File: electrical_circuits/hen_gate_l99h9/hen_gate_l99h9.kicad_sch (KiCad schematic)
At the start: 4 parts, among them U1 L99H02XP

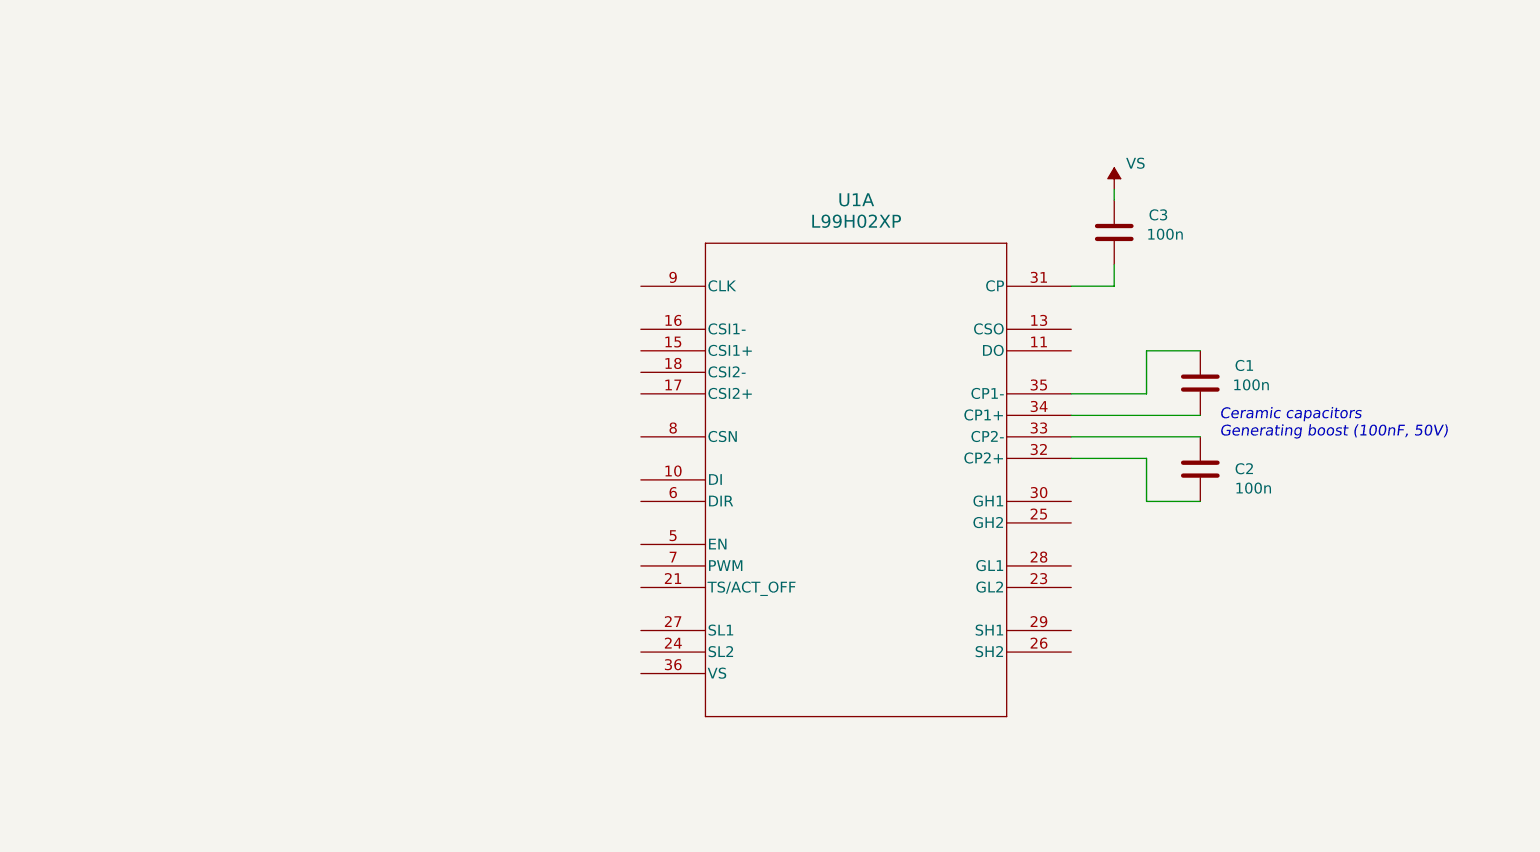
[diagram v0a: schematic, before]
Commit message: Chosen MOSFET transistors and other elements for LT1158 gate driver.
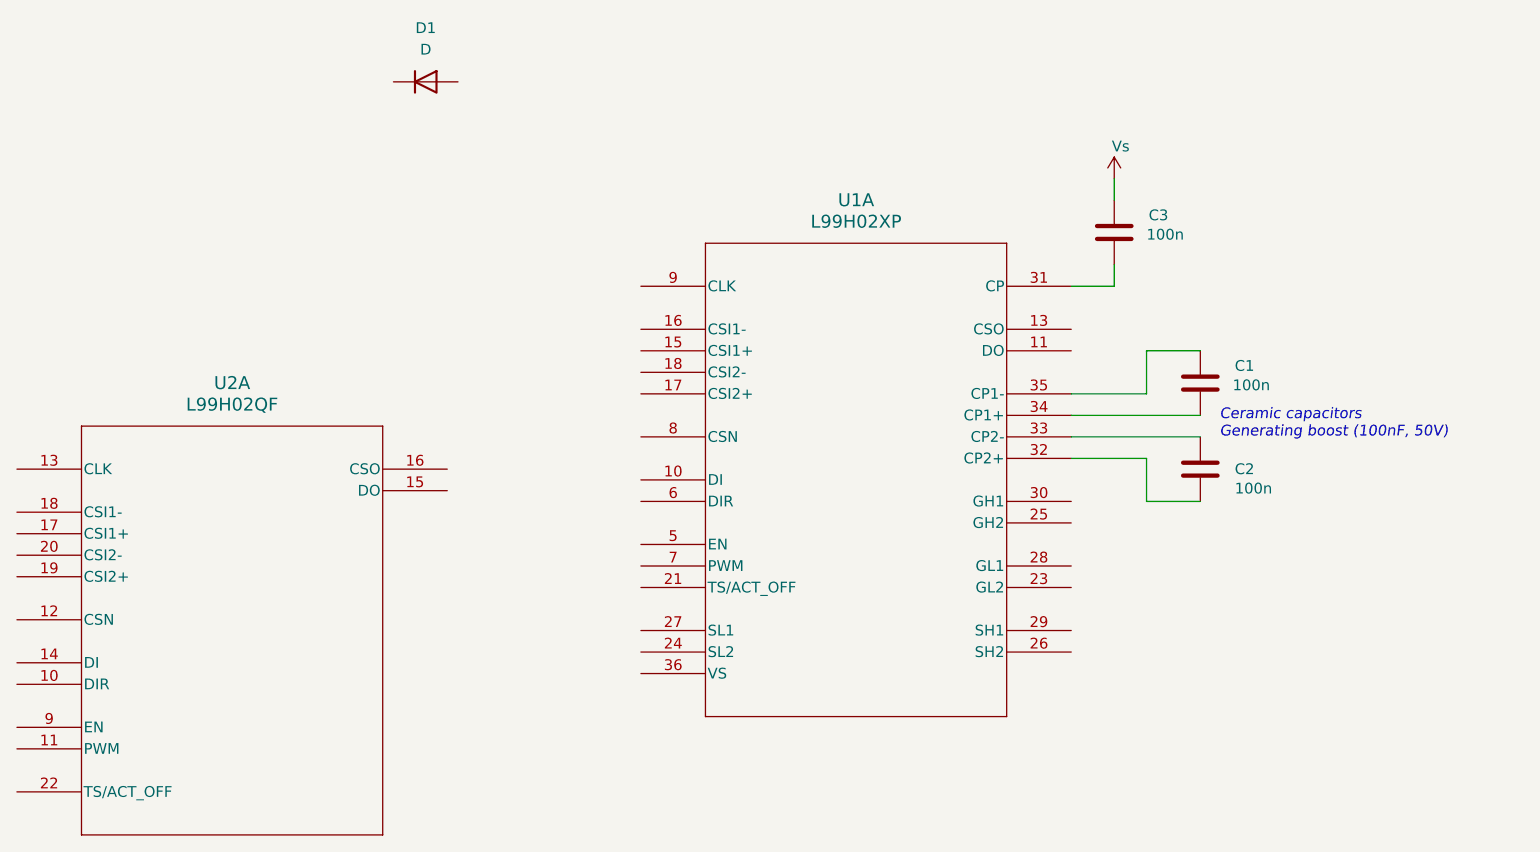
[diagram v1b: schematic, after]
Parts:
- added D1: D, symbol Device:D
- added U2: L99H02QF, L99H02QF:LQFP32_STM, symbol L99H02QF:L99H02QF
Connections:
- net VS renamed Vs
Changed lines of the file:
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@@
-	(wire
-		(pts
-			(xy 218.44 62.23) (xy 218.44 63.5)
-		)
-		(stroke
-			(width 0)
-			(type default)
-		)
-	)
 	(wire
 		(pts
@@
 		(pts
 			(xy 213.36 91.44) (xy 228.6 91.44)
+		)
+		(stroke
+			(width 0)
+			(type default)
+		)
+	)
+	(wire
+		(pts
+			(xy 218.44 60.96) (xy 218.44 63.5)
 		)
 		(stroke
@@
 	)
 	(symbol
+		(lib_id "power:+3.3V")
+		(at 218.44 60.96 0)
+		(unit 1)
+		(exclude_from_sim no)
+		(in_bom yes)
+		(on_board yes)
+		(dnp no)
+		(property "Reference" "#PWR1"
+			(at 218.44 64.77 0)
+			(effects
+				(font
+					(size 1.27 1.27)
+				)
+				(hide yes)
+			)
+		)
+		(property "Value" "Vs"
+			(at 219.202 57.15 0)
+			(effects
+				(font
+					(size 1.27 1.27)
+				)
+			)
+		)
+		(property "Footprint" ""
+			(at 218.44 60.96 0)
+			(effects
+				(font
+					(size 1.27 1.27)
+				)
+				(hide yes)
+			)
+		)
+		(property "Datasheet" ""
+			(at 218.44 60.96 0)
+			(effects
+				(font
+					(size 1.27 1.27)
+				)
+				(hide yes)
+			)
+		)
+		(property "Description" "Power symbol creates a global label with name \"+3.3V\""
+			(at 218.44 60.96 0)
+			(effects
+				(font
+					(size 1.27 1.27)
+				)
+				(hide yes)
+			)
+		)
+		(pin "1"
+		)
+		(instances
+			(project ""
+				(path "/635bc36b-05ec-41d6-a641-f3afe2a34102"
+					(reference "#PWR1")
+					(unit 1)
+				)
+			)
+		)
+	)
+	(symbol
 		(lib_id "Device:C")
 		(at 228.6 85.09 0)
@@
 	)
 	(symbol
-		(lib_id "power:VS")
-		(at 218.44 62.23 0)
+		(lib_id "L99H02QF:L99H02QF")
+		(at 88.9 95.25 0)
 		(unit 1)
 		(exclude_from_sim no)
@@
 		(on_board yes)
 		(dnp no)
-		(property "Reference" "#PWR1"
-			(at 218.44 66.04 0)
-			(effects
-				(font
-					(size 1.27 1.27)
-				)
-				(hide yes)
-			)
-		)
-		(property "Value" "VS"
-			(at 220.98 59.182 0)
-			(effects
-				(font
-					(size 1.27 1.27)
-				)
-			)
-		)
-		(property "Footprint" ""
-			(at 218.44 62.23 0)
-			(effects
-				(font
-					(size 1.27 1.27)
-				)
-				(hide yes)
-			)
-		)
-		(property "Datasheet" ""
-			(at 218.44 62.23 0)
-			(effects
-				(font
-					(size 1.27 1.27)
-				)
-				(hide yes)
-			)
-		)
-		(property "Description" "Power symbol creates a global label with name \"VS\""
-			(at 218.44 62.23 0)
-			(effects
-				(font
-					(size 1.27 1.27)
-				)
-				(hide yes)
-			)
+		(fields_autoplaced yes)
+		(property "Reference" "U2"
+			(at 114.3 85.09 0)
+			(effects
+				(font
+					(size 1.524 1.524)
+				)
+			)
+		)
+		(property "Value" "L99H02QF"
+			(at 114.3 87.63 0)
+			(effects
+				(font
+					(size 1.524 1.524)
+				)
+			)
+		)
+		(property "Footprint" "L99H02QF:LQFP32_STM"
+			(at 88.9 95.25 0)
+			(effects
+				(font
+					(size 1.27 1.27)
+					(italic yes)
+				)
+				(hide yes)
+			)
+		)
+		(property "Datasheet" "L99H02QF"
+			(at 88.9 95.25 0)
+			(effects
+				(font
+					(size 1.27 1.27)
+					(italic yes)
+				)
+				(hide yes)
+			)
+		)
+		(property "Description" ""
+			(at 88.9 95.25 0)
+			(effects
+				(font
+					(size 1.27 1.27)
+				)
+				(hide yes)
+			)
+		)
+		(pin "19"
+		)
+		(pin "20"
+		)
+		(pin "22"
+		)
+		(pin "3"
+		)
+		(pin "18"
+		)
+		(pin "11"
+		)
+		(pin "15"
+		)
+		(pin "16"
+		)
+		(pin "12"
+		)
+		(pin "29"
+		)
+		(pin "7"
+		)
+		(pin "14"
+		)
+		(pin "6"
+		)
+		(pin "9"
+		)
+		(pin "31"
+		)
+		(pin "23"
+		)
+		(pin "8"
+		)
+		(pin "4"
+		)
+		(pin "27"
+		)
+		(pin "32"
+		)
+		(pin "21"
+		)
+		(pin "28"
+		)
+		(pin "2"
+		)
+		(pin "24"
+		)
+		(pin "25"
+		)
+		(pin "5"
+		)
+		(pin "26"
+		)
+		(pin "30"
+		)
+		(pin "13"
+		)
+		(pin "17"
+		)
+		(pin "10"
 		)
 		(pin "1"
@@
 			(project ""
 				(path "/635bc36b-05ec-41d6-a641-f3afe2a34102"
-					(reference "#PWR1")
+					(reference "U2")
 					(unit 1)
 				)
@@
 					(unit 1)
 				)
+			)
+		)
+	)
+	(symbol
+		(lib_id "Device:D")
+		(at 137.16 49.53 0)
+		(unit 1)
+		(exclude_from_sim no)
+		(in_bom yes)
+		(on_board yes)
+		(dnp no)
+		(fields_autoplaced yes)
+		(property "Reference" "D1"
+			(at 137.16 43.18 0)
+			(effects
+				(font
+					(size 1.27 1.27)
+				)
+			)
+		)
+		(property "Value" "D"
+			(at 137.16 45.72 0)
+			(effects
+				(font
+					(size 1.27 1.27)
+				)
+			)
+		)
+		(property "Footprint" ""
+			(at 137.16 49.53 0)
+			(effects
+				(font
+					(size 1.27 1.27)
+				)
+				(hide yes)
+			)
+		)
+		(property "Datasheet" "~"
+			(at 137.16 49.53 0)
+			(effects
+				(font
+					(size 1.27 1.27)
+				)
+				(hide yes)
+			)
+		)
+		(property "Description" "STTH8R06D"
+			(at 137.16 49.53 0)
+			(effects
+				(font
+					(size 1.27 1.27)
+				)
+				(hide yes)
+			)
+		)
+		(property "Sim.Device" "D"
+			(at 137.16 49.53 0)
+			(effects
+				(font
+					(size 1.27 1.27)
+				)
+				(hide yes)
+			)
+		)
+		(property "Sim.Pins" "1=K 2=A"
+			(at 137.16 49.53 0)
+			(effects
+				(font
+					(size 1.27 1.27)
+				)
+				(hide yes)
+			)
+		)
+		(pin "1"
+		)
+		(pin "2"
+		)
+		(instances
+			(project ""
+				(path "/635bc36b-05ec-41d6-a641-f3afe2a34102"
+					(reference "D1")
+					(unit 1)
+				)
